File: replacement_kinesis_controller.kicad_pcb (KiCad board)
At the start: 2 copper layers, 99.1 x 86.4 mm, 74 parts, among them CN1 USB_general, CN4 USB_general, K1 CONN_3, K2 CONN_3, K3 CONN_3, K4 CONN_3, P1 CONN_3X2, P15 CONN_5X2, P16 CONN_16, P17 CONN_16, P18 POWER, P19 PCM, P2 CONN_13, P20 UART, P21 SPI, P22 IO, P23 SMIRF, P3 CONN_13, P4 CONN_10, P5 CONN_10, P6 CONN_13, P7 CONN_13, P8 CONN_5X2, P9 CONN_6, SW3 SPST, SW4 SPST, U1 MCP23018-E, U9 MCP1700

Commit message: Spread out components
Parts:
- moved C20 146.6 mm to (262.9, 95.2)
- moved C19 145.4 mm to (264.2, 104.1)
- moved C11 145.1 mm to (266.7, 161.3)
- moved C12 144.1 mm to (266.7, 152.4)
- moved C13 143.7 mm to (266.7, 146.1)
- moved C18 143.5 mm to (264.2, 113.0)
- moved C17 142.4 mm to (264.2, 119.4)
- moved C15 142.4 mm to (265.4, 133.3)
- moved C14 142.2 mm to (265.4, 139.7)
- moved C16 141.6 mm to (264.2, 125.7)
- moved C1 139.2 mm to (250.2, 82.5)
- moved C2 134.9 mm to (250.2, 94.0)
- moved C3 131.9 mm to (250.2, 104.1)
- moved C4 129.7 mm to (250.2, 113.0)
- moved C10 128.6 mm to (250.2, 160.0)
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
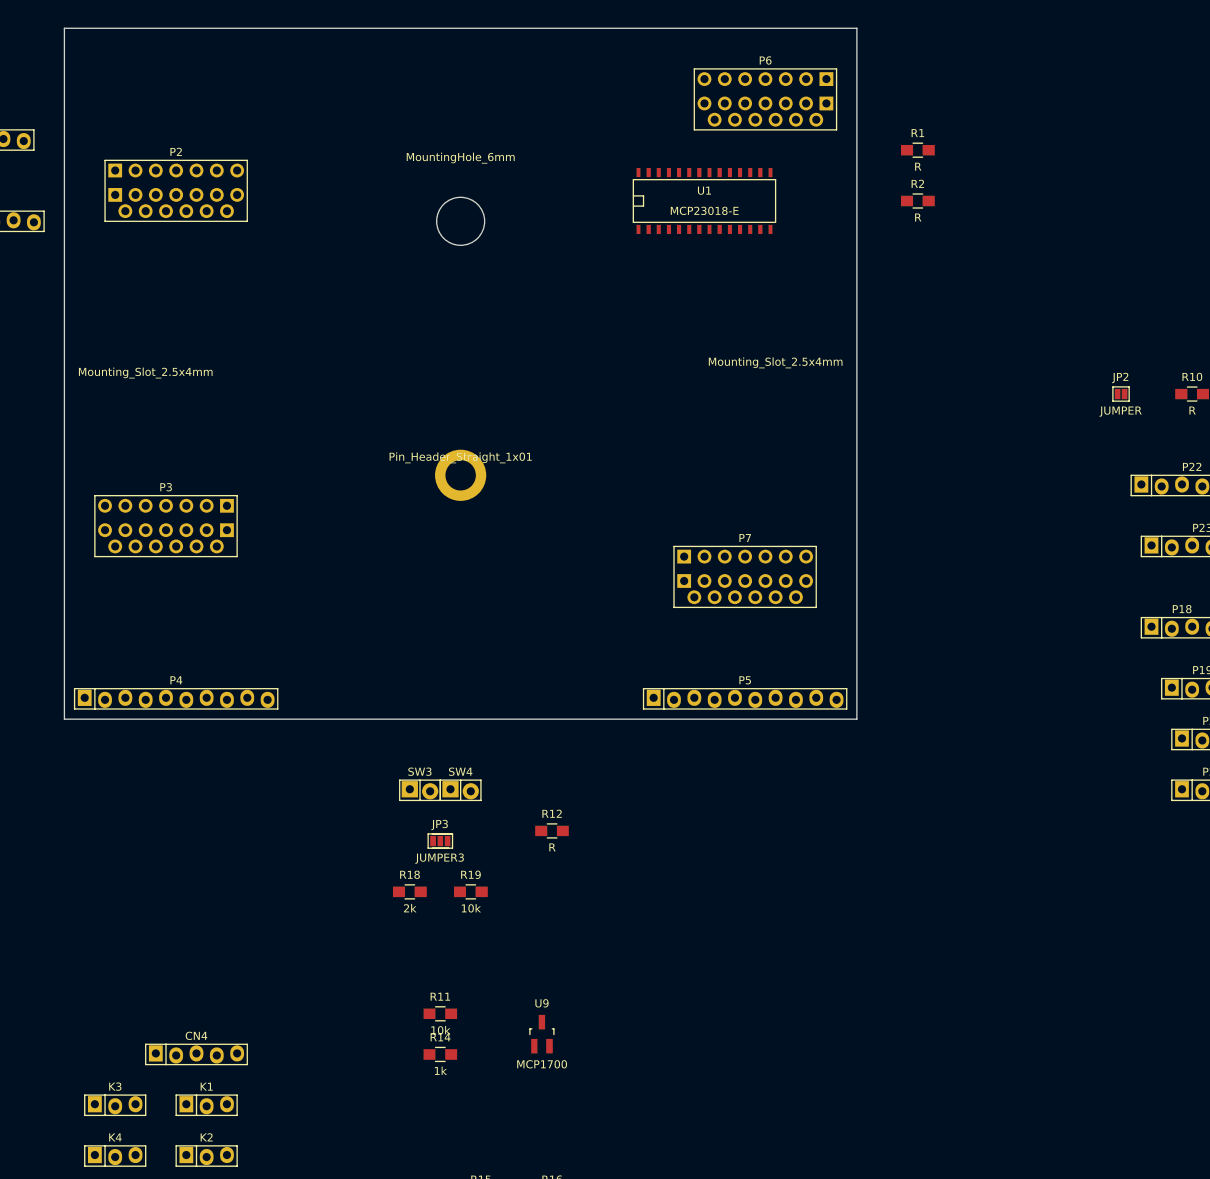
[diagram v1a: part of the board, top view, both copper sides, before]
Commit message: Matrix connectors in place
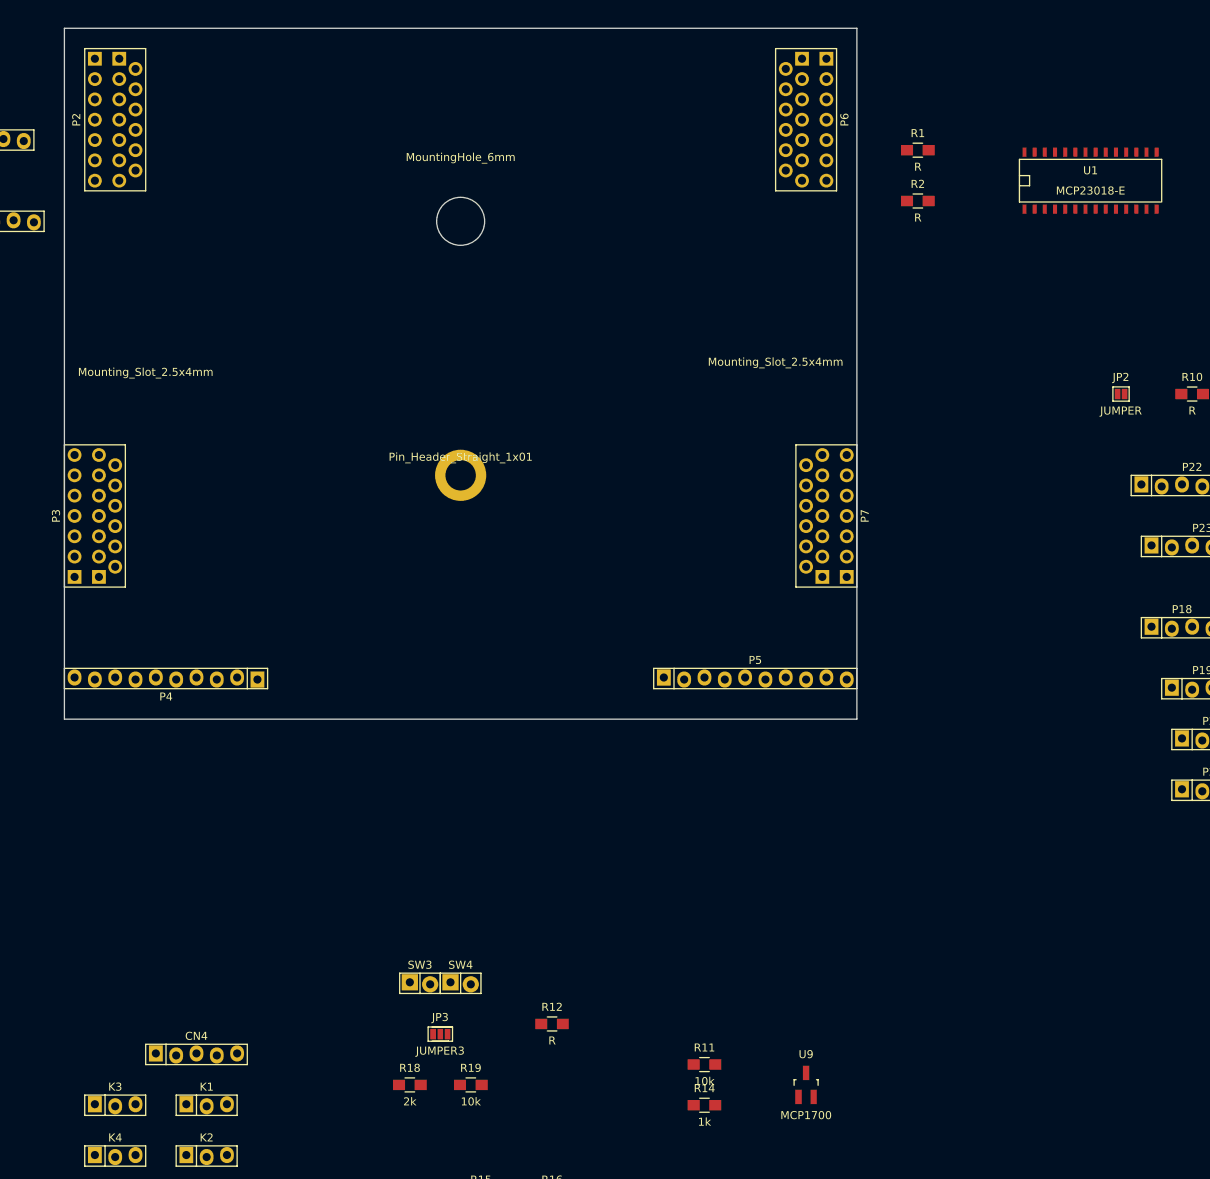
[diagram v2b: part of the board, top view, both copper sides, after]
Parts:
- P2, P7: footprint replacement_kinesis_controller:Molex_FFC_13 -> replacement_kinesis_controller:Molex_FFC_13_mirror
- P3, P6: footprint replacement_kinesis_controller:Molex_FFC_13_mirror -> replacement_kinesis_controller:Molex_FFC_13
- moved U1 48.3 mm to (201.9, 62.2)
- moved U9 33.6 mm to (166.4, 175.3)
- moved R11 33.6 mm to (153.7, 172.7)
- moved R14 33.6 mm to (153.7, 177.8)
- moved JP3 24.1 mm to (120.7, 168.9)
- moved R12 24.1 mm to (134.6, 167.6)
- moved R18 24.1 mm to (116.8, 175.3)
- moved R19 24.1 mm to (124.5, 175.3)
- moved SW3 24.1 mm to (118.1, 162.6)
- moved SW4 24.1 mm to (123.2, 162.6)
- moved P7 12.7 mm to (168.9, 104.1), turned to 270 degrees
- moved P2 11.7 mm to (80.0, 54.6), turned to 90 degrees
- moved P3 8.98 mm to (77.5, 104.1), turned to 90 degrees
- moved P6 5.68 mm to (166.4, 54.6), turned to 270 degrees
- moved P5 2.84 mm to (160.0, 124.5)
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
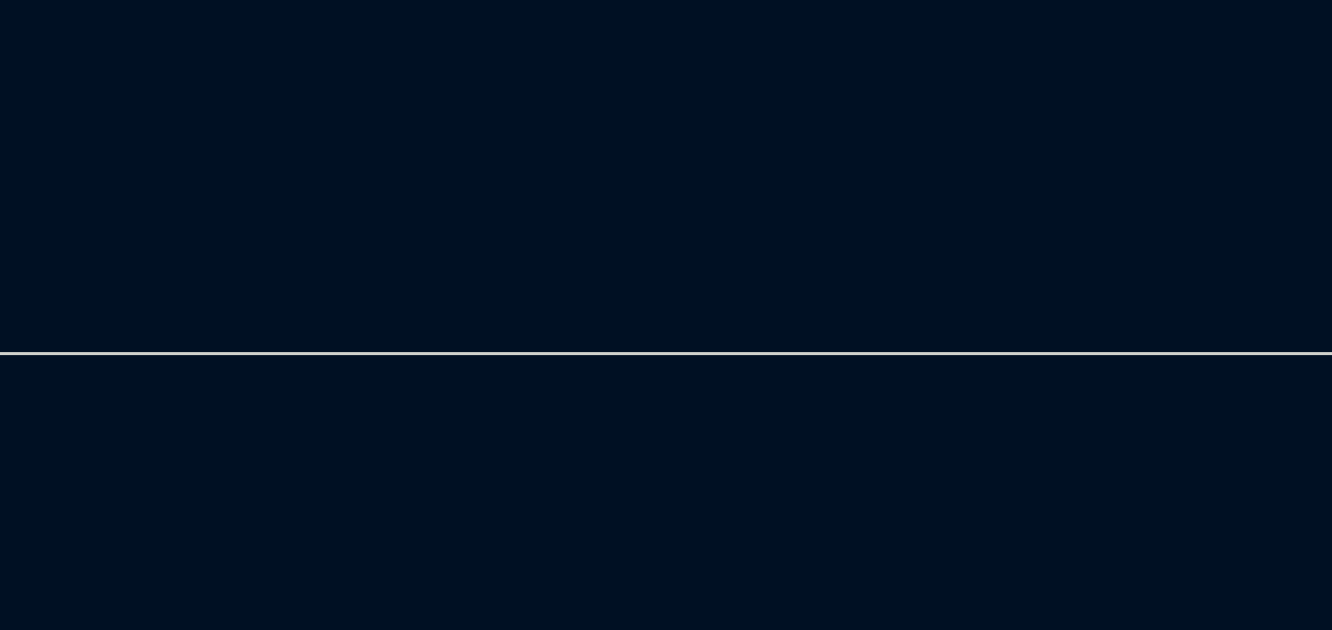
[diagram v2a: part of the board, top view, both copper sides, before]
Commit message: Add RGB LEDs
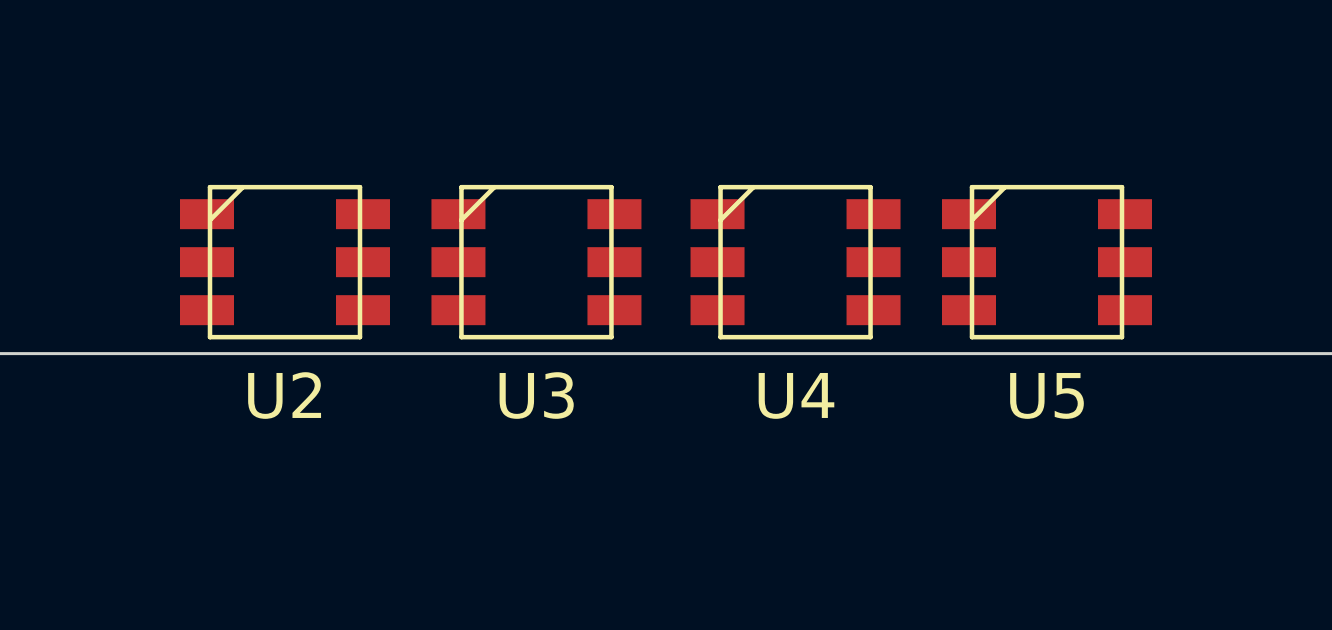
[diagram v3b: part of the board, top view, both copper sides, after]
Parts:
- added U2: WS2811_RGB_LED, replacement_kinesis_controller:LED_RGB_WS2811, F.Cu at (110.5, 126.5)
- added U3: WS2811_RGB_LED, replacement_kinesis_controller:LED_RGB_WS2811, F.Cu at (118.9, 126.5)
- added U4: WS2811_RGB_LED, replacement_kinesis_controller:LED_RGB_WS2811, F.Cu at (127.5, 126.5)
- added U5: WS2811_RGB_LED, replacement_kinesis_controller:LED_RGB_WS2811, F.Cu at (135.9, 126.5)
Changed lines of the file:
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@@
 (kicad_pcb (version 4) (host pcbnew "(2015-02-21 BZR 5441)-product")
   (general
-    (links 208)
-    (no_connects 208)
+    (links 224)
+    (no_connects 224)
     (area 73.609999 43.129999 172.770001 129.590001)
     (thickness 1.6)
@@
     (tracks 0)
     (zones 0)
-    (modules 74)
-    (nets 114)
+    (modules 78)
+    (nets 122)
   )
   (page A4)
@@
   (net 112 "Net-(U1-Pad17)")
   (net 113 "Net-(U1-Pad28)")
+  (net 114 "Net-(U2-Pad4)")
+  (net 115 "Net-(U2-Pad1)")
+  (net 116 "Net-(U3-Pad4)")
+  (net 117 "Net-(U3-Pad1)")
+  (net 118 "Net-(U4-Pad4)")
+  (net 119 "Net-(U4-Pad1)")
+  (net 120 "Net-(U5-Pad4)")
+  (net 121 LED_OUT)
   (net_class Default "This is the default net class."
     (clearance 0.254)
@@
     (add_net INTA)
     (add_net INTB)
+    (add_net LED_OUT)
     (add_net "Net-(C15-Pad1)")
     (add_net "Net-(C18-Pad1)")
@@
     (add_net "Net-(U1-Pad2)")
     (add_net "Net-(U1-Pad28)")
+    (add_net "Net-(U2-Pad1)")
+    (add_net "Net-(U2-Pad4)")
+    (add_net "Net-(U3-Pad1)")
+    (add_net "Net-(U3-Pad4)")
+    (add_net "Net-(U4-Pad1)")
+    (add_net "Net-(U4-Pad4)")
+    (add_net "Net-(U5-Pad4)")
     (add_net PB0)
     (add_net PB4)
@@
     )
     (pad 1 thru_hole circle (at 0 0) (size 6.4 6.4) (drill 3.8) (layers *.Cu *.Mask F.SilkS))
-    (model Pin_Headers/Pin_Header_Straight_1x01.wrl
-      (at (xyz 0 0 0))
-      (scale (xyz 1 1 1))
-      (rotate (xyz 0 0 0))
-    )
   )
   (module replacement_kinesis_controller:Mounting_Slot_2.5x4mm (layer F.Cu)
@@
     )
   )
+  (module replacement_kinesis_controller:LED_RGB_WS2811 (layer F.Cu)
+    (at 110.49 126.492)
+    (fp_text reference U2 (at 0 4.5) (layer F.SilkS)
+      (effects (font (size 1.5 1.5) (thickness 0.15)))
+    )
+    (fp_text value WS2811_RGB_LED (at 0 -4.4) (layer F.Fab)
+      (effects (font (size 1.5 1.5) (thickness 0.15)))
+    )
+    (fp_line (start -1.4 -2.5) (end -2.5 -1.4) (layer F.SilkS) (width 0.15))
+    (fp_line (start -2.5 -2.5) (end 2.5 -2.5) (layer F.SilkS) (width 0.15))
+    (fp_line (start 2.5 -2.5) (end 2.5 2.5) (layer F.SilkS) (width 0.15))
+    (fp_line (start 2.5 2.5) (end -2.5 2.5) (layer F.SilkS) (width 0.15))
+    (fp_line (start -2.5 2.5) (end -2.5 -2.5) (layer F.SilkS) (width 0.15))
+    (pad 5 smd rect (at 2.6 0) (size 1.8 1) (layers F.Cu F.Paste F.Mask)
+      (net 1 VCC))
+    (pad 4 smd rect (at 2.6 -1.6) (size 1.8 1) (layers F.Cu F.Paste F.Mask)
+      (net 114 "Net-(U2-Pad4)"))
+    (pad 6 smd rect (at 2.6 1.6) (size 1.8 1) (layers F.Cu F.Paste F.Mask)
+      (net 2 GND))
+    (pad 3 smd rect (at -2.6 1.6) (size 1.8 1) (layers F.Cu F.Paste F.Mask)
+      (net 1 VCC))
+    (pad 1 smd rect (at -2.6 -1.6) (size 1.8 1) (layers F.Cu F.Paste F.Mask)
+      (net 115 "Net-(U2-Pad1)"))
+    (pad 2 smd rect (at -2.6 0) (size 1.8 1) (layers F.Cu F.Paste F.Mask)
+      (net 70 PD4))
+  )
+  (module replacement_kinesis_controller:LED_RGB_WS2811 (layer F.Cu)
+    (at 118.872 126.492)
+    (fp_text reference U3 (at 0 4.5) (layer F.SilkS)
+      (effects (font (size 1.5 1.5) (thickness 0.15)))
+    )
+    (fp_text value WS2811_RGB_LED (at 0 -4.4) (layer F.Fab)
+      (effects (font (size 1.5 1.5) (thickness 0.15)))
+    )
+    (fp_line (start -1.4 -2.5) (end -2.5 -1.4) (layer F.SilkS) (width 0.15))
+    (fp_line (start -2.5 -2.5) (end 2.5 -2.5) (layer F.SilkS) (width 0.15))
+    (fp_line (start 2.5 -2.5) (end 2.5 2.5) (layer F.SilkS) (width 0.15))
+    (fp_line (start 2.5 2.5) (end -2.5 2.5) (layer F.SilkS) (width 0.15))
+    (fp_line (start -2.5 2.5) (end -2.5 -2.5) (layer F.SilkS) (width 0.15))
+    (pad 5 smd rect (at 2.6 0) (size 1.8 1) (layers F.Cu F.Paste F.Mask)
+      (net 1 VCC))
+    (pad 4 smd rect (at 2.6 -1.6) (size 1.8 1) (layers F.Cu F.Paste F.Mask)
+      (net 116 "Net-(U3-Pad4)"))
+    (pad 6 smd rect (at 2.6 1.6) (size 1.8 1) (layers F.Cu F.Paste F.Mask)
+      (net 2 GND))
+    (pad 3 smd rect (at -2.6 1.6) (size 1.8 1) (layers F.Cu F.Paste F.Mask)
+      (net 1 VCC))
+    (pad 1 smd rect (at -2.6 -1.6) (size 1.8 1) (layers F.Cu F.Paste F.Mask)
+      (net 117 "Net-(U3-Pad1)"))
+    (pad 2 smd rect (at -2.6 0) (size 1.8 1) (layers F.Cu F.Paste F.Mask)
+      (net 115 "Net-(U2-Pad1)"))
+  )
+  (module replacement_kinesis_controller:LED_RGB_WS2811 (layer F.Cu)
+    (at 127.508 126.492)
+    (fp_text reference U4 (at 0 4.5) (layer F.SilkS)
+      (effects (font (size 1.5 1.5) (thickness 0.15)))
+    )
+    (fp_text value WS2811_RGB_LED (at 0 -4.4) (layer F.Fab)
+      (effects (font (size 1.5 1.5) (thickness 0.15)))
+    )
+    (fp_line (start -1.4 -2.5) (end -2.5 -1.4) (layer F.SilkS) (width 0.15))
+    (fp_line (start -2.5 -2.5) (end 2.5 -2.5) (layer F.SilkS) (width 0.15))
+    (fp_line (start 2.5 -2.5) (end 2.5 2.5) (layer F.SilkS) (width 0.15))
+    (fp_line (start 2.5 2.5) (end -2.5 2.5) (layer F.SilkS) (width 0.15))
+    (fp_line (start -2.5 2.5) (end -2.5 -2.5) (layer F.SilkS) (width 0.15))
+    (pad 5 smd rect (at 2.6 0) (size 1.8 1) (layers F.Cu F.Paste F.Mask)
+      (net 1 VCC))
+    (pad 4 smd rect (at 2.6 -1.6) (size 1.8 1) (layers F.Cu F.Paste F.Mask)
+      (net 118 "Net-(U4-Pad4)"))
+    (pad 6 smd rect (at 2.6 1.6) (size 1.8 1) (layers F.Cu F.Paste F.Mask)
+      (net 2 GND))
+    (pad 3 smd rect (at -2.6 1.6) (size 1.8 1) (layers F.Cu F.Paste F.Mask)
+      (net 1 VCC))
+    (pad 1 smd rect (at -2.6 -1.6) (size 1.8 1) (layers F.Cu F.Paste F.Mask)
+      (net 119 "Net-(U4-Pad1)"))
+    (pad 2 smd rect (at -2.6 0) (size 1.8 1) (layers F.Cu F.Paste F.Mask)
+      (net 117 "Net-(U3-Pad1)"))
+  )
+  (module replacement_kinesis_controller:LED_RGB_WS2811 (layer F.Cu)
+    (at 135.89 126.492)
+    (fp_text reference U5 (at 0 4.5) (layer F.SilkS)
+      (effects (font (size 1.5 1.5) (thickness 0.15)))
+    )
+    (fp_text value WS2811_RGB_LED (at 0 -4.4) (layer F.Fab)
+      (effects (font (size 1.5 1.5) (thickness 0.15)))
+    )
+    (fp_line (start -1.4 -2.5) (end -2.5 -1.4) (layer F.SilkS) (width 0.15))
+    (fp_line (start -2.5 -2.5) (end 2.5 -2.5) (layer F.SilkS) (width 0.15))
+    (fp_line (start 2.5 -2.5) (end 2.5 2.5) (layer F.SilkS) (width 0.15))
+    (fp_line (start 2.5 2.5) (end -2.5 2.5) (layer F.SilkS) (width 0.15))
+    (fp_line (start -2.5 2.5) (end -2.5 -2.5) (layer F.SilkS) (width 0.15))
+    (pad 5 smd rect (at 2.6 0) (size 1.8 1) (layers F.Cu F.Paste F.Mask)
+      (net 1 VCC))
+    (pad 4 smd rect (at 2.6 -1.6) (size 1.8 1) (layers F.Cu F.Paste F.Mask)
+      (net 120 "Net-(U5-Pad4)"))
+    (pad 6 smd rect (at 2.6 1.6) (size 1.8 1) (layers F.Cu F.Paste F.Mask)
+      (net 2 GND))
+    (pad 3 smd rect (at -2.6 1.6) (size 1.8 1) (layers F.Cu F.Paste F.Mask)
+      (net 1 VCC))
+    (pad 1 smd rect (at -2.6 -1.6) (size 1.8 1) (layers F.Cu F.Paste F.Mask)
+      (net 121 LED_OUT))
+    (pad 2 smd rect (at -2.6 0) (size 1.8 1) (layers F.Cu F.Paste F.Mask)
+      (net 119 "Net-(U4-Pad1)"))
+  )
   (gr_line (start 73.66 129.54) (end 73.66 43.18) (angle 90) (layer Edge.Cuts) (width 0.1))

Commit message: Some changes to PCB
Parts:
- moved P16 63.5 mm to (110.5, 74.9), turned to 90 degrees
- moved P1 55.7 mm to (100.3, 53.3)
- moved U1 54.7 mm to (147.3, 66.0), turned to 270 degrees
- moved P17 40.1 mm to (90.2, 74.9), turned to 270 degrees
- moved R8 34.2 mm to (34.3, 21.6)
- moved JP1 26.9 mm to (26.7, 104.1)
- moved R9 23.4 mm to (41.9, 22.9)
- moved CN1 18.2 mm to (31.8, 120.7)
- moved R3 18.2 mm to (58.4, 108.0)
- moved R4 18.2 mm to (58.4, 114.3)
- moved R5 18.2 mm to (34.3, 104.1)
- moved R7 18.2 mm to (52.1, 120.7)
- moved R6 18.2 mm to (44.5, 115.6)
